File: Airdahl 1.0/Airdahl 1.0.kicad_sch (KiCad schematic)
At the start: 29 parts, among them J1 Conn_ARM_JTAG_SWD_20, SW1 SW_MEC_5E, U1 STM32F446RETx, X2 ABS25-32.768KHZ-6-T, Y1 ABM3B-8.000MHZ-12-D1X-T

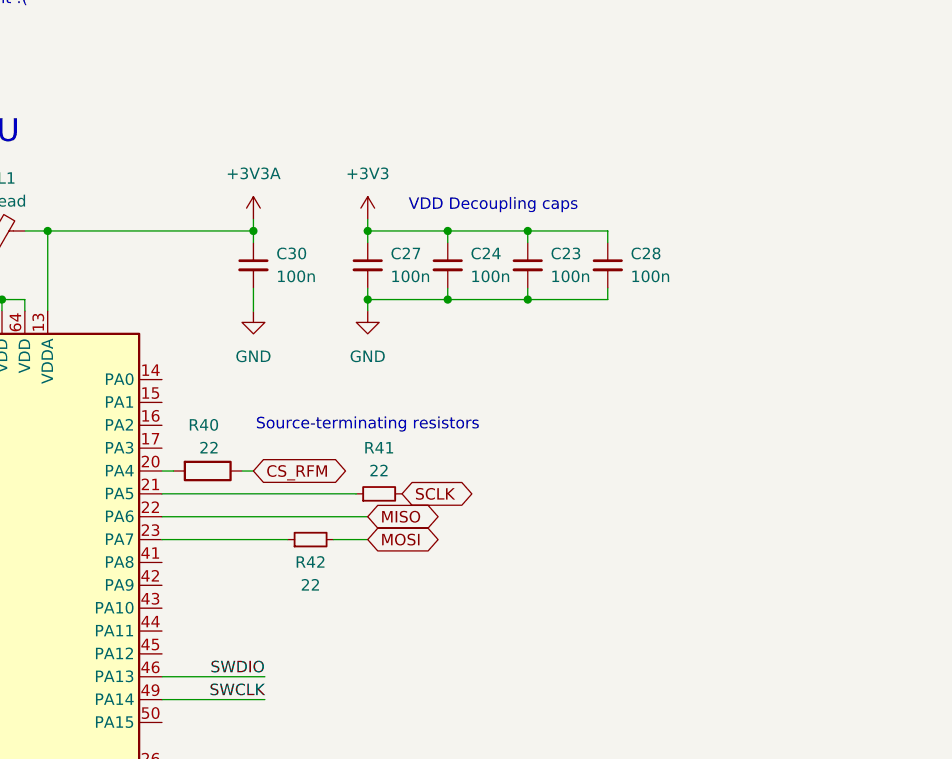
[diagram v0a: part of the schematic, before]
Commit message: added missing decoupling caps and fixed mcu resistor footprints
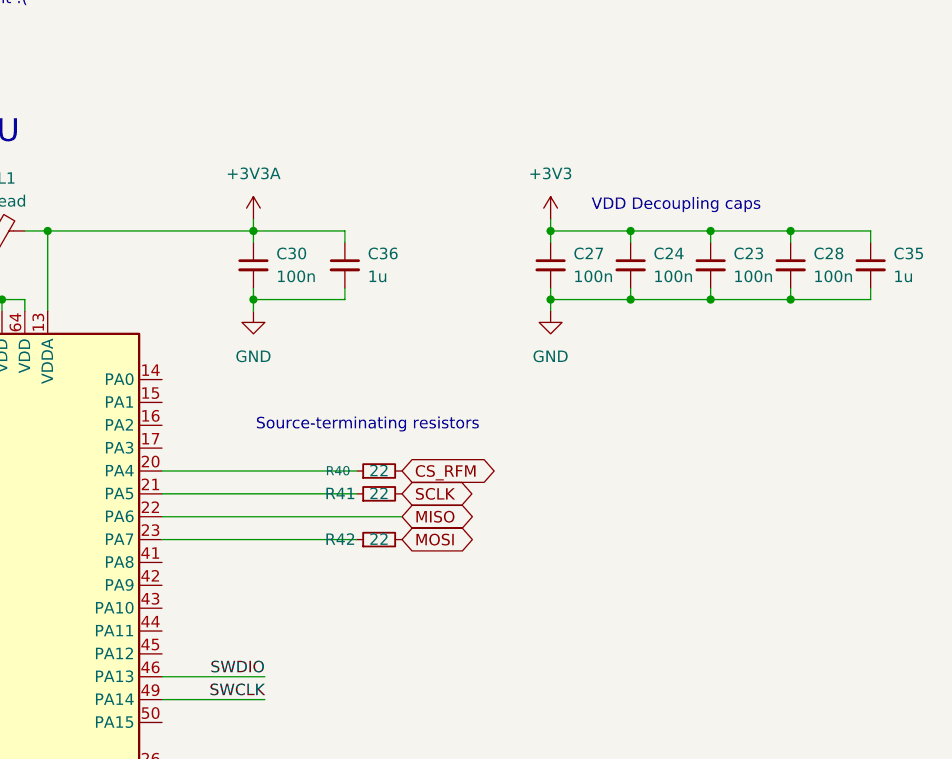
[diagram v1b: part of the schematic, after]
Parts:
- removed R40: 22, Resistor_SMD:R_0402_1005Metric, symbol Device:R
- added C35, C36: 1u, Capacitor_SMD:C_0603_1608Metric_Pad1.08x0.95mm_HandSolder, symbol Device:C_Small
- added R40: 22, Resistor_SMD:R_0402_1005Metric, symbol Device:R_Small
- R17, R18, R33, R34, R35, R36, R37, R41, R42: footprint Resistor_SMD:R_0201_0603Metric_Pad0.64x0.40mm_HandSolder -> Resistor_SMD:R_0402_1005Metric
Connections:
- net +3V3: now also C35.1
- net +3V3A: now also C36.1
- net CS_RFM: now also R40.2
- net GND: now also C35.2, C36.2
- net at U1.20 (PA4): now also R40.1
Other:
- moved on the sheet: C23, C24, C27, C28, R42

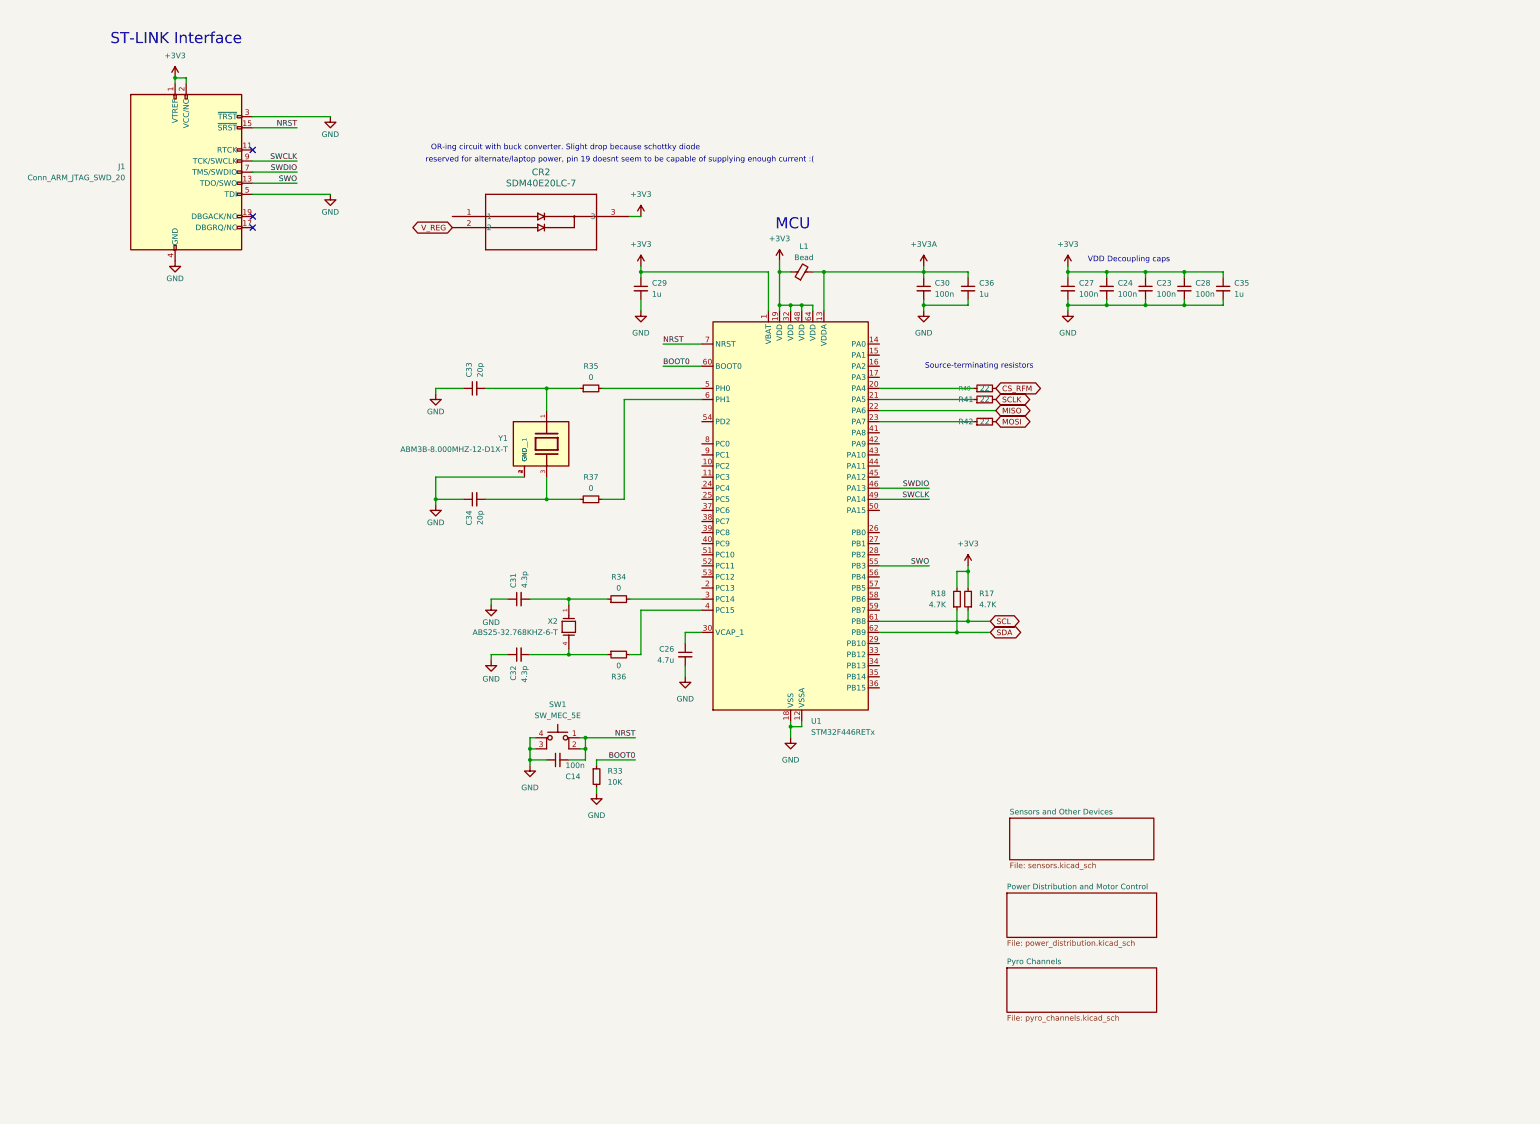
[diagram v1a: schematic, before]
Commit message: restructured airdahl for carrier boards, switched 20 pin debug jtag for 10 pin for use with adafruit usb stlink, schematic formatting
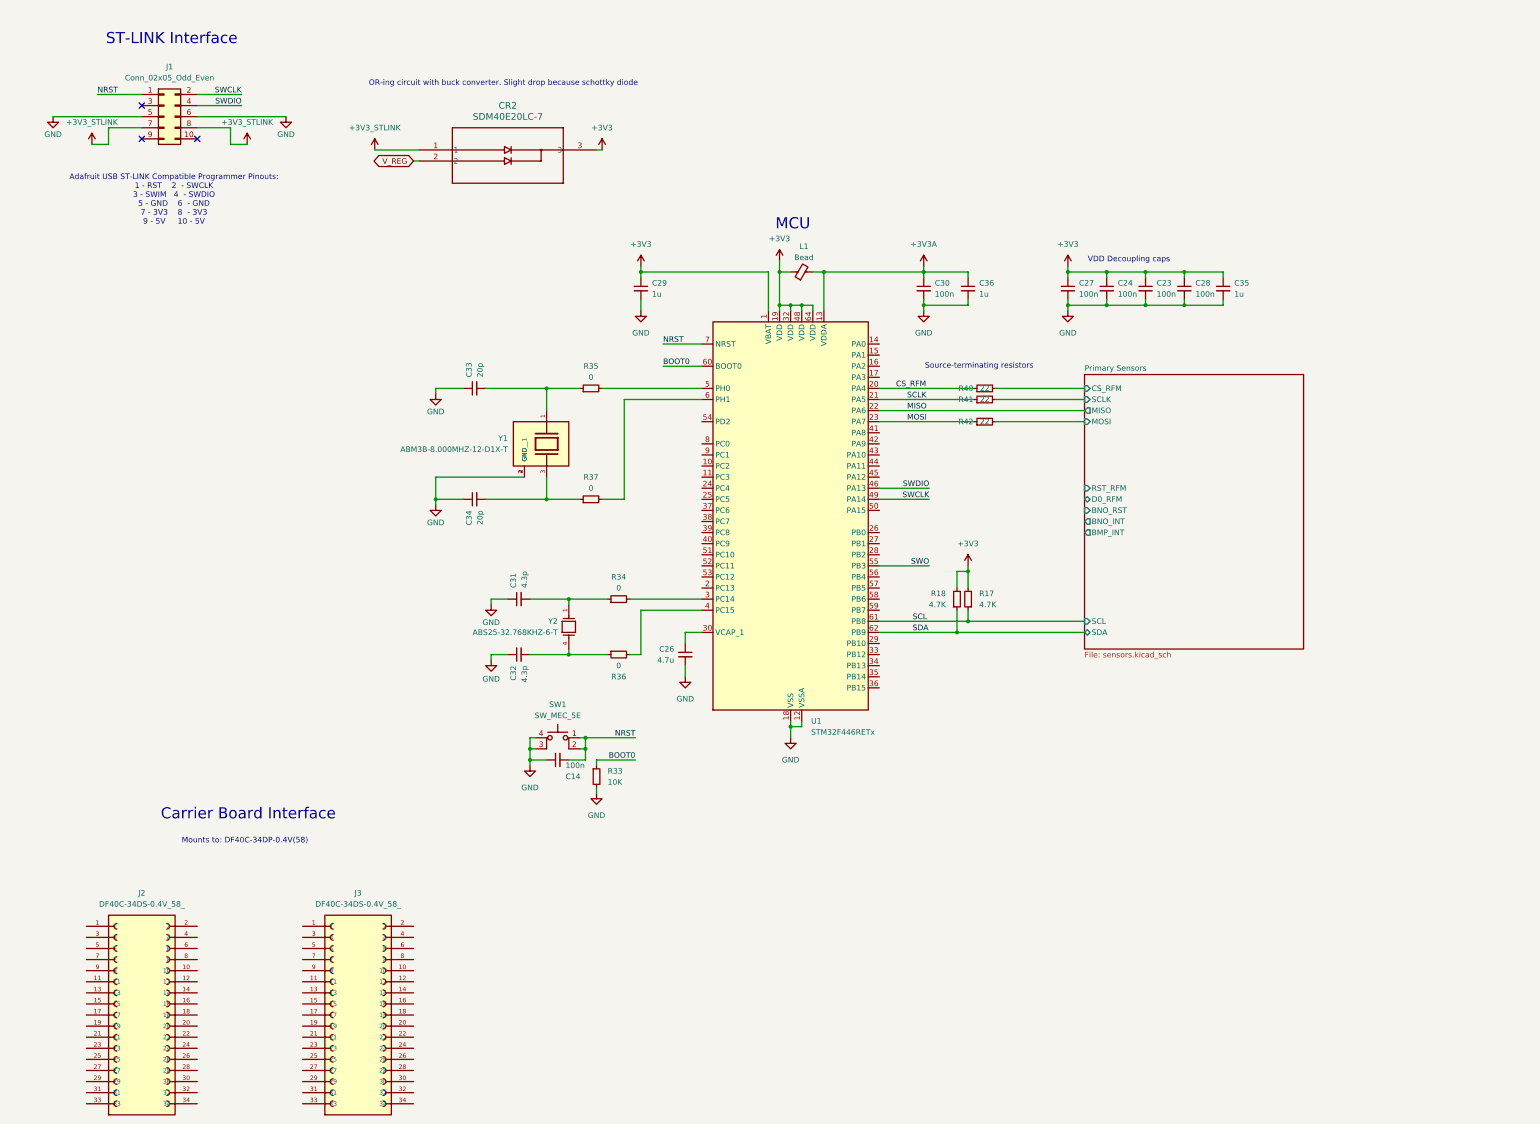
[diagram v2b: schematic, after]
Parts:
- removed J1: Conn_ARM_JTAG_SWD_20, Connector_IDC:IDC-Header_2x10_P2.54mm_Vertical, symbol Connector:Conn_ARM_JTAG_SWD_20
- added J1: Conn_02x05_Odd_Even, 3220-10-0100:CONN_3220-10-0100-00_CNC, symbol Connector_Generic:Conn_02x05_Odd_Even
- added J2, J3: DF40C-34DS-0.4V_58_, DF40C-34DS-0.4V_58_:HIROSE_DF40C-34DS-0.4V_58_, symbol DF40C-34DS-0.4V_58_:DF40C-34DS-0.4V_58_
- renumbered X2 to Y2
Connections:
- net CS_RFM: now also R40.1, U1.20 (PA4); no longer R40.2
- net GND: now also J1.5 (Pin_5), J1.6 (Pin_6)
- net MOSI: now also R42.1, U1.23 (PA7); no longer R42.2
- net NRST: now also J1.1 (Pin_1)
- net SCLK: now also R41.1, U1.21 (PA5); no longer R41.2
- net SWCLK: now also J1.2 (Pin_2)
- net SWDIO: now also J1.4 (Pin_4)
- net +3V3_STLINK: now reaches CR2.1
- net +3V3_STLINK: now also J1.7 (Pin_7), J1.8 (Pin_8)
- new net Primary Sensors/CS_RFM: R40.2
- new net Primary Sensors/MOSI: R42.2
- new net Primary Sensors/SCLK: R41.2
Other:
- sheet Sensors and Other Devices renamed Primary Sensors
- removed sheet Power Distribution and Motor Control
- removed sheet Pyro Channels
- sheet Primary Sensors ports: added BMP_INT, BNO_INT, BNO_RST, CS_RFM, D0_RFM, MISO, MOSI, RST_RFM, SCL, SCLK, SDA; removed none
- note added: "Adafruit USB ST-LINK Compatible Programmer Pinouts: 1 - RST 2 - SWCLK 3 - SWIM 4 - SWDIO 5 - GND 6 - GND 7 - 3V3 8 - 3V3 9 - 5V 10 - 5V"
- note added: "Carrier Board Interface"
- note added: "Mounts to: DF40C-34DP-0.4V(58)"
- note removed: "reserved for alternate/laptop power, pin 19 doesnt seem to be capable of supplying enough current :("
- company: (none) -> Washington University in St. Louis
- title: AirDahl Flight Computer -> AirDahl Flight Computer Mainboard
- moved on the sheet: CR2

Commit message: swd and uart interfaces for mainboard, updated power or-ing circuit
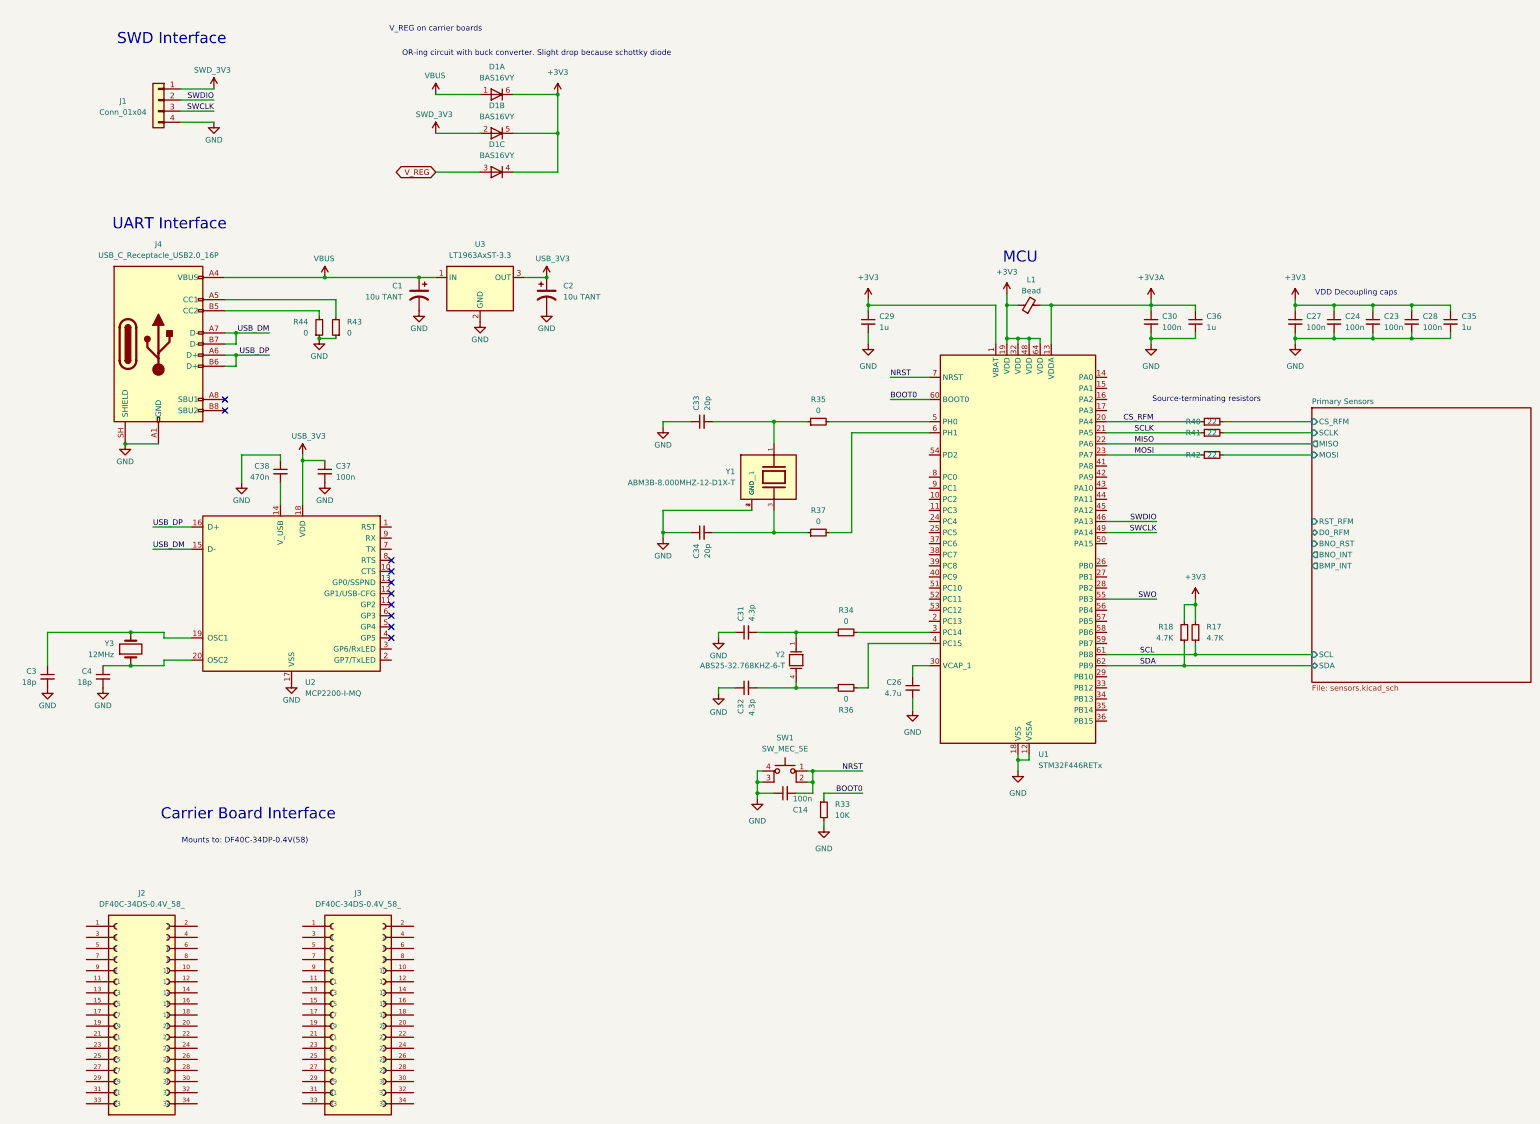
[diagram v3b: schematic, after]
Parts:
- removed CR2: SDM40E20LC-7, SOT-23_DIO, symbol SDM40E20LC_7:SDM40E20LC-7
- removed J1: Conn_02x05_Odd_Even, 3220-10-0100:CONN_3220-10-0100-00_CNC, symbol Connector_Generic:Conn_02x05_Odd_Even
- added C1, C2: 10u TANT, Capacitor_SMD:C_1206_3216Metric, symbol Device:C_Polarized_US
- added C3, C4: 18p, Capacitor_SMD:C_0402_1005Metric, symbol Device:C_Small
- added C37: 100n, Capacitor_SMD:C_0603_1608Metric_Pad1.08x0.95mm_HandSolder, symbol Device:C_Small
- added C38: 470n, Capacitor_SMD:C_0603_1608Metric_Pad1.08x0.95mm_HandSolder, symbol Device:C_Small
- added D1: BAS16VY, Package_TO_SOT_SMD:SOT-363_SC-70-6, symbol Diode:BAS16VY
- added J1: Conn_01x04, Connector_PinHeader_2.54mm:PinHeader_1x04_P2.54mm_Vertical, symbol Connector_Generic:Conn_01x04
- added J4: USB_C_Receptacle_USB2.0_16P, Connector_USB:USB_C_Receptacle_GCT_USB4105-xx-A_16P_TopMnt_Horizontal, symbol Connector:USB_C_Receptacle_USB2.0_16P
- added R43, R44: 0, Resistor_SMD:R_0402_1005Metric, symbol Device:R_Small
- added U2: MCP2200-I-MQ, Package_DFN_QFN:QFN-20-1EP_5x5mm_P0.65mm_EP3.35x3.35mm, symbol Interface_USB:MCP2200-I-MQ
- added U3: LT1963AxST-3.3, Package_TO_SOT_SMD:SOT-223-3_TabPin2, symbol Regulator_Linear:LT1963AxST-3.3
- added Y3: 12MHz, Crystal:Crystal_HC49-4H_Vertical, symbol Device:Crystal
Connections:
- net +3V3: now also D1.4 (K), D1.5 (K), D1.6 (K)
- net GND: now also C1.2, C2.2, C3.2, C37.2, C38.1, C4.2, J1.4 (Pin_4), J4.A1 (GND), J4.A12 (GND), J4.B1 (GND), J4.B12 (GND), J4.SH (SHIELD), R43.1, R44.1, U2.17 (VSS), U3.2 (GND)
- net SWCLK: now also J1.3 (Pin_3)
- net SWDIO: now also J1.2 (Pin_2)
- net V_REG: now also D1.3 (A)
- new net: C38.2, U2.14 (V_USB)
- new net: C3.1, U2.19 (OSC1), Y3.2
- new net: C4.1, U2.20 (OSC2), Y3.1
- new net: J4.A5 (CC1), R43.2
- new net: J4.B5 (CC2), R44.2
- new net SWD_3V3: D1.2 (A), J1.1 (Pin_1)
- new net USB_3V3: C2.1, C37.1, U2.18 (VDD), U3.3 (OUT)
- new net USB_DM: J4.A7 (D-), J4.B7 (D-), U2.15 (D-)
- new net USB_DP: J4.A6 (D+), J4.B6 (D+), U2.16 (D+)
- new net VBUS: C1.1, D1.1 (A), J4.A4 (VBUS), J4.A9 (VBUS), J4.B4 (VBUS), J4.B9 (VBUS), U3.1 (IN)
- no-connect marks 3 -> 10
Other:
- note added: "SWD Interface"
- note added: "UART Interface"
- note added: "V_REG on carrier boards"
- note removed: "Adafruit USB ST-LINK Compatible Programmer Pinouts: 1 - RST 2 - SWCLK 3 - SWIM 4 - SWDIO 5 - GND 6 - GND 7 - 3V3 8 - 3V3 9 - 5V 10 - 5V"
- note removed: "ST-LINK Interface"
- moved on the sheet: C14, C23, C24, C26, C27, C28, C29, C30, C31, C32, C33, C34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

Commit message: fixed usbc cc pins, boot0 button, uart connections
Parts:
- added C15: 100n, Capacitor_SMD:C_0603_1608Metric_Pad1.08x0.95mm_HandSolder, symbol Device:C_Small
- added SW2: SW_MEC_5E, Button_Switch_SMD:SW_MEC_5GSH9, symbol Switch:SW_MEC_5E
- R43, R44: value 0 -> 5.1k
- Y3: footprint Crystal:Crystal_HC49-4H_Vertical -> Crystal:Crystal_SMD_Abracon_ABM3-2Pin_5.0x3.2mm
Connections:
- net +3V3: now also C15.1, SW2.3 (K), SW2.4 (A)
- net BOOT0: now also C15.2, SW2.1, SW2.2
- net UART_TX: now reaches U2.7 (TX)
- net UART_TX: now also U1.52 (PC11)
- net UART_RX: now reaches U2.9 (RX)
- net UART_RX: now also U1.51 (PC10)
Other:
- note added: "RX: PC10 TX: PC11"
- moved on the sheet: R33
